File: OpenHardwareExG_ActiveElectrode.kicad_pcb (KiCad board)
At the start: 2 copper layers, 19.1 x 19.1 mm, 13 parts, among them K1 CONN_3, P1 CONN_1, U1 LMP7715, U2 LMP7721

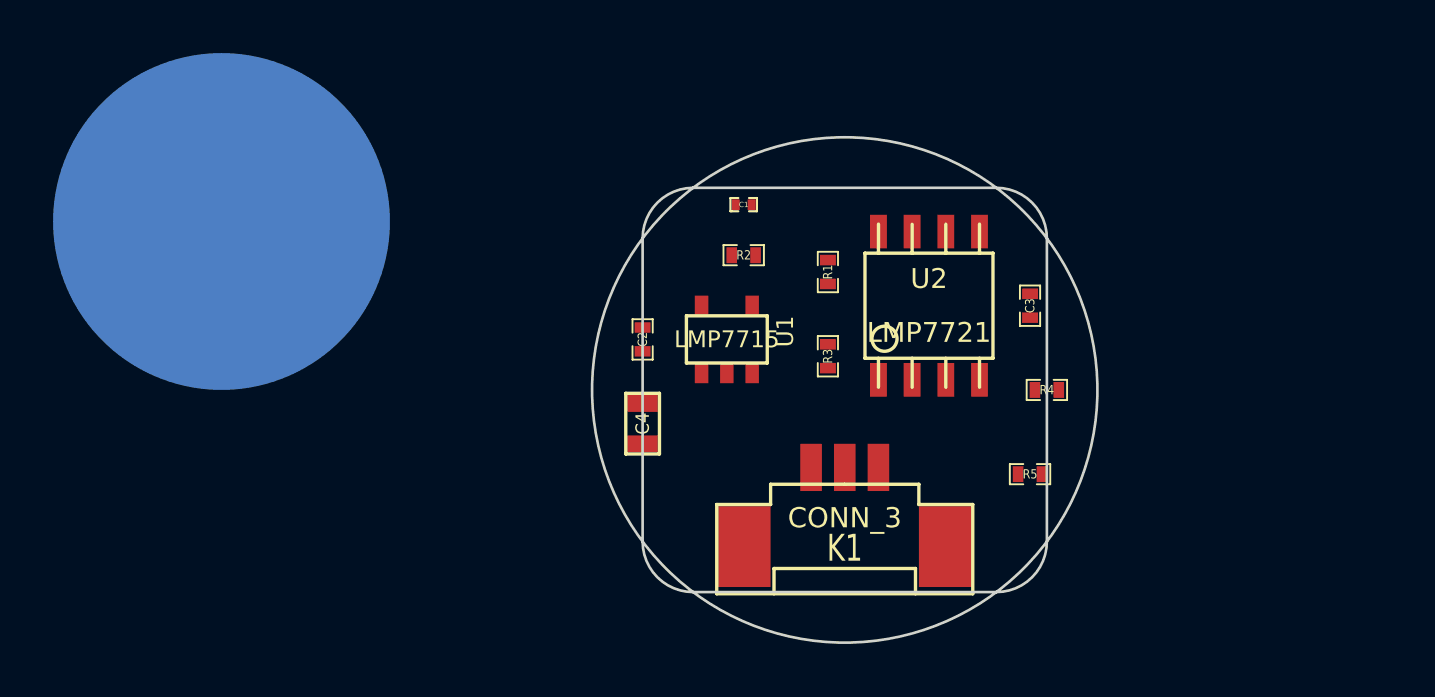
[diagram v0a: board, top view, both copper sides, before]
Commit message: improved draft of component positions
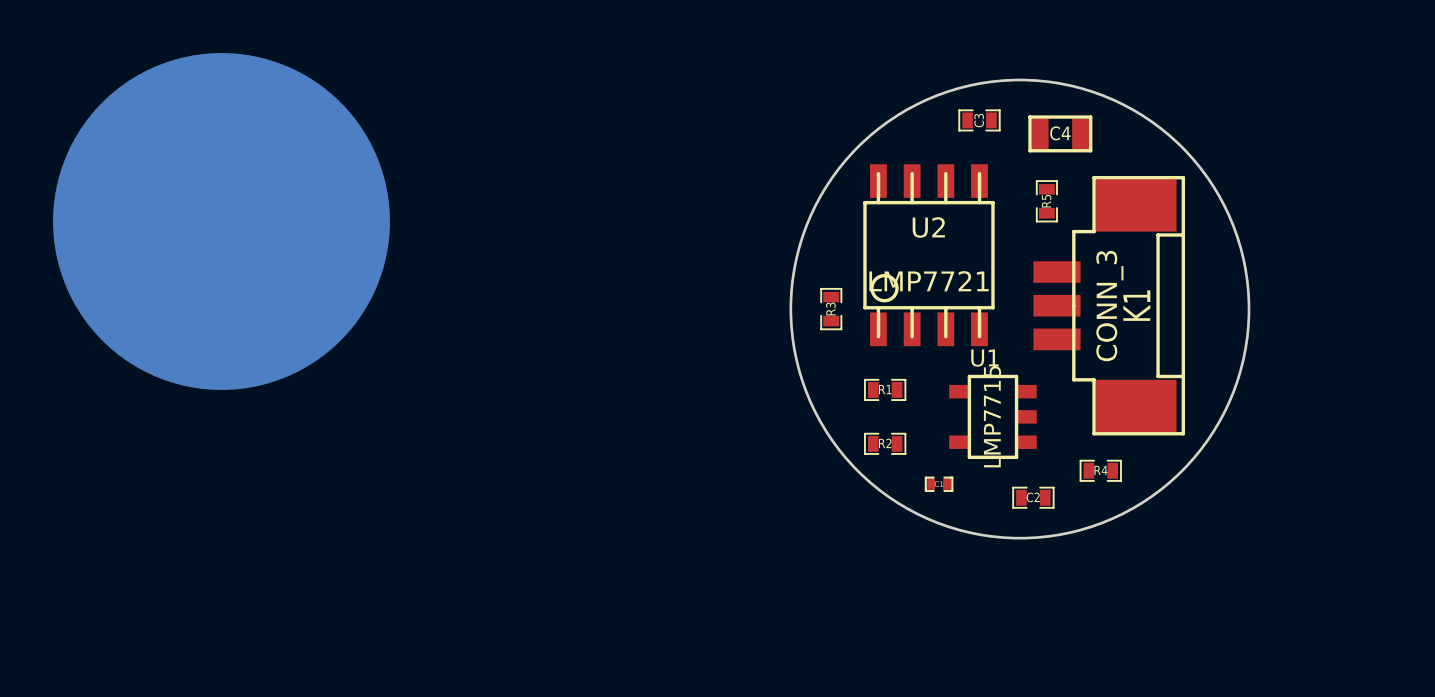
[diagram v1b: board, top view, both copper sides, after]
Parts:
- moved C4 19.2 mm to (109.7, 43.7), turned to 0 degrees
- moved C2 15.9 mm to (108.7, 57.4), turned to 0 degrees
- moved K1 14.9 mm to (113.0, 50.2), turned to 90 degrees
- moved C1 12.9 mm to (105.2, 56.9), turned to 0 degrees
- moved U1 10.4 mm to (107.2, 54.4), turned to 90 degrees
- moved R5 10.3 mm to (109.2, 46.2), turned to 270 degrees
- moved R2 8.89 mm to (103.1, 55.4), turned to 0 degrees
- moved C3 7.24 mm to (106.7, 43.2), turned to 0 degrees
- moved R1 4.94 mm to (103.1, 53.3), turned to 180 degrees
- moved R4 3.66 mm to (111.3, 56.4)
- moved U2 1.91 mm to (104.8, 48.3)
- moved R3 1.78 mm to (101.1, 50.3), turned to 270 degrees
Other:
- board size 19.1 x 19.1 mm -> 17.3 x 17.3 mm

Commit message: experiment with 0.1" connector (too large)
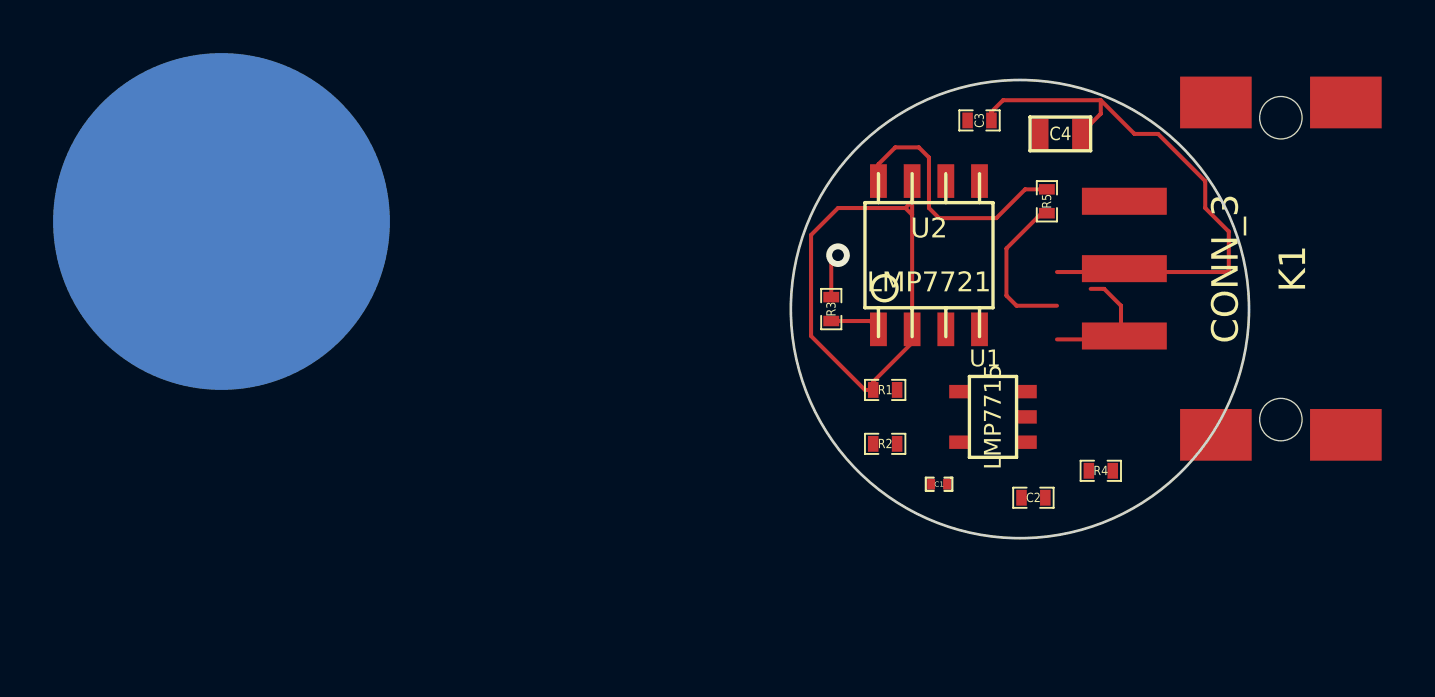
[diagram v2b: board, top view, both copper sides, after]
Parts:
- K1: footprint CONN3_SMD -> 3PIN_SMD_ERNI
- moved K1 1.66 mm to (112.1, 48.8), turned to 270 degrees
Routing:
- net GND: track 0.00 -> 26.6 mm
- net /GUARD_RING: track 0.00 -> 20.9 mm
- net /BUFFERED_INPUT: track 0.00 -> 9.92 mm
- net /LINE_OUT: track 0.00 -> 5.92 mm
- net /PROTECTED_ELECTRODE: track 0.00 -> 1.91 mm
- net /ELECTRODE: track 0.00 -> 1.69 mm, vias 0 -> 1
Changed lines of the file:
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@@
   (general
     (links 24)
-    (no_connects 24)
+    (no_connects 19)
     (area 0 0 0 0)
     (thickness 1.6)
     (drawings 1)
-    (tracks 0)
+    (tracks 49)
     (zones 0)
     (modules 13)
@@
     (mod_text_size 1 1)
     (mod_text_width 0.15)
-    (pad_size 12.7 12.7)
-    (pad_drill 0)
+    (pad_size 1.6 1.6)
+    (pad_drill 1.6)
     (pad_to_mask_clearance 0)
     (aux_axis_origin 0 0)
@@
     )
   )
-  (module CONN3_SMD (layer F.Cu)
-    (at 113.03 50.165 90)
-    (attr smd)
-    (fp_text reference K1 (at 0 -0.381 90) (layer F.SilkS)
-      (effects (font (size 1.016 0.762) (thickness 0.1524)))
-    )
-    (fp_text value CONN_3 (at 0 -1.524 90) (layer F.SilkS)
-      (effects (font (size 0.762 0.762) (thickness 0.1524)))
-    )
-    (fp_line (start 2.667 1.3335) (end 2.667 0.381) (layer F.SilkS) (width 0.127))
-    (fp_line (start 2.667 0.381) (end -2.667 0.381) (layer F.SilkS) (width 0.127))
-    (fp_line (start -2.667 0.381) (end -2.667 1.3335) (layer F.SilkS) (width 0.127))
-    (fp_line (start 0 -2.794) (end 2.794 -2.794) (layer F.SilkS) (width 0.127))
-    (fp_line (start 2.794 -2.794) (end 2.794 -2.032) (layer F.SilkS) (width 0.127))
-    (fp_line (start 2.794 -2.032) (end 4.826 -2.032) (layer F.SilkS) (width 0.127))
-    (fp_line (start 4.826 -2.032) (end 4.826 1.3335) (layer F.SilkS) (width 0.127))
-    (fp_line (start 4.826 1.3335) (end -4.826 1.3335) (layer F.SilkS) (width 0.127))
-    (fp_line (start -4.826 1.3335) (end -4.826 -2.032) (layer F.SilkS) (width 0.127))
-    (fp_line (start -4.826 -2.032) (end -2.794 -2.032) (layer F.SilkS) (width 0.127))
-    (fp_line (start -2.794 -2.032) (end -2.794 -2.794) (layer F.SilkS) (width 0.127))
-    (fp_line (start -2.794 -2.794) (end 0 -2.794) (layer F.SilkS) (width 0.127))
-    (pad 3 smd rect (at 1.27 -3.429 90) (size 0.8128 1.778)
-      (layers F.Cu F.Paste F.Mask)
-      (net 10 GND)
-    )
-    (pad 2 smd rect (at 0 -3.429 90) (size 0.8128 1.778)
-      (layers F.Cu F.Paste F.Mask)
-      (net 8 /LINE_OUT)
-    )
-    (pad 1 smd rect (at -1.27 -3.429 90) (size 0.8128 1.778)
-      (layers F.Cu F.Paste F.Mask)
-      (net 1 +5V)
-    )
-    (pad "" smd rect (at 3.81 -0.4445 90) (size 2.032 3.048)
-      (layers F.Cu F.Paste F.Mask)
-    )
-    (pad "" smd rect (at -3.81 -0.4445 90) (size 2.032 3.048)
-      (layers F.Cu F.Paste F.Mask)
-    )
-    (model smd/conn3_smd.wrl
-      (at (xyz 0 0 0))
-      (scale (xyz 0.4 0.4 0.4))
-      (rotate (xyz 0 0 0))
-    )
-  )
   (module electrode_pad (layer B.Cu)
     (at 78.105 46.99)
@@
     )
   )
+  (module 3PIN_SMD_ERNI (layer F.Cu)
+    (at 112.141 48.768 270)
+    (fp_text reference K1 (at 0 -6.35 270) (layer F.SilkS)
+      (effects (font (size 1 1) (thickness 0.15)))
+    )
+    (fp_text value CONN_3 (at 0 -3.81 270) (layer F.SilkS)
+      (effects (font (size 1 1) (thickness 0.15)))
+    )
+    (pad 2 smd rect (at 0 0 270) (size 1.02 3.2)
+      (layers F.Cu F.Paste F.Mask)
+      (net 8 /LINE_OUT)
+    )
+    (pad 3 smd rect (at 2.54 0 270) (size 1.02 3.2)
+      (layers F.Cu F.Paste F.Mask)
+      (net 10 GND)
+    )
+    (pad 1 smd rect (at -2.54 0 270) (size 1.02 3.2)
+      (layers F.Cu F.Paste F.Mask)
+      (net 1 +5V)
+    )
+    (pad "" smd rect (at -6.265 -3.45 270) (size 1.95 2.7)
+      (layers F.Cu F.Paste F.Mask)
+    )
+    (pad "" smd rect (at 6.265 -3.45 270) (size 1.95 2.7)
+      (layers F.Cu F.Paste F.Mask)
+    )
+    (pad "" smd rect (at -6.265 -8.35 270) (size 1.95 2.7)
+      (layers F.Cu F.Paste F.Mask)
+    )
+    (pad "" smd rect (at 6.265 -8.35 270) (size 1.95 2.7)
+      (layers F.Cu F.Paste F.Mask)
+    )
+    (pad "" np_thru_hole circle (at -5.69 -5.9 270) (size 1.6 1.6) (drill 1.6)
+      (layers *.Cu *.Mask F.SilkS)
+    )
+    (pad "" np_thru_hole circle (at 5.69 -5.9 270) (size 1.6 1.6) (drill 1.6)
+      (layers *.Cu *.Mask F.SilkS)
+    )
+  )
   (gr_circle (center 108.204 50.292) (end 108.204 58.928) (layer Edge.Cuts) (width 0.1))
+  (segment (start 102.87 45.466) (end 102.87 44.831) (width 0.1524) (layer F.Cu) (net 2))
+  (segment (start 108.39958 45.77842) (end 109.22 45.77842) (width 0.1524) (layer F.Cu) (net 2))
+  (segment (start 107.315 46.863) (end 108.39958 45.77842) (width 0.1524) (layer F.Cu) (net 2))
+  (segment (start 105.156 46.863) (end 107.315 46.863) (width 0.1524) (layer F.Cu) (net 2))
+  (segment (start 104.775 46.482) (end 105.156 46.863) (width 0.1524) (layer F.Cu) (net 2))
+  (segment (start 104.775 44.577) (end 104.775 46.482) (width 0.1524) (layer F.Cu) (net 2))
+  (segment (start 104.394 44.196) (end 104.775 44.577) (width 0.1524) (layer F.Cu) (net 2))
+  (segment (start 103.505 44.196) (end 104.394 44.196) (width 0.1524) (layer F.Cu) (net 2))
+  (segment (start 102.87 44.831) (end 103.505 44.196) (width 0.1524) (layer F.Cu) (net 2))
+  (segment (start 101.092 49.84242) (end 101.092 48.514) (width 0.1524) (layer F.Cu) (net 3))
+  (via (at 101.346 48.26) (size 0.889) (layers F.Cu B.Cu) (net 3))
+  (segment (start 101.092 48.514) (end 101.346 48.26) (width 0.1524) (layer F.Cu) (net 3))
+  (segment (start 103.886 46.482) (end 104.14 46.736) (width 0.1524) (layer F.Cu) (net 4))
+  (segment (start 104.14 51.054) (end 104.14 46.736) (width 0.1524) (layer F.Cu) (net 4))
+  (segment (start 104.14 46.736) (end 104.14 45.466) (width 0.1524) (layer F.Cu) (net 4))
+  (segment (start 102.67442 53.34) (end 102.362 53.34) (width 0.1524) (layer F.Cu) (net 4))
+  (segment (start 102.362 53.34) (end 100.33 51.308) (width 0.1524) (layer F.Cu) (net 4))
+  (segment (start 100.33 51.308) (end 100.33 47.498) (width 0.1524) (layer F.Cu) (net 4))
+  (segment (start 100.33 47.498) (end 101.346 46.482) (width 0.1524) (layer F.Cu) (net 4))
+  (segment (start 101.346 46.482) (end 103.886 46.482) (width 0.1524) (layer F.Cu) (net 4))
+  (segment (start 103.886 46.482) (end 104.14 46.228) (width 0.1524) (layer F.Cu) (net 4))
+  (segment (start 104.14 46.228) (end 104.14 45.466) (width 0.1524) (layer F.Cu) (net 4))
+  (segment (start 104.14 51.054) (end 104.14 51.562) (width 0.1524) (layer F.Cu) (net 4))
+  (segment (start 102.67442 53.02758) (end 102.67442 53.34) (width 0.1524) (layer F.Cu) (net 4))
+  (segment (start 104.14 51.562) (end 102.67442 53.02758) (width 0.1524) (layer F.Cu) (net 4))
+  (segment (start 109.22 46.67758) (end 109.02442 46.67758) (width 0.1524) (layer F.Cu) (net 8))
+  (segment (start 108.077 50.165) (end 109.601 50.165) (width 0.1524) (layer F.Cu) (net 8))
+  (segment (start 107.696 49.784) (end 108.077 50.165) (width 0.1524) (layer F.Cu) (net 8))
+  (segment (start 107.696 48.006) (end 107.696 49.784) (width 0.1524) (layer F.Cu) (net 8))
+  (segment (start 109.02442 46.67758) (end 107.696 48.006) (width 0.1524) (layer F.Cu) (net 8))
+  (segment (start 101.092 50.74158) (end 102.55758 50.74158) (width 0.1524) (layer F.Cu) (net 9))
+  (segment (start 102.55758 50.74158) (end 102.87 51.054) (width 0.1524) (layer F.Cu) (net 9))
+  (segment (start 109.601 51.435) (end 111.633 51.435) (width 0.1524) (layer F.Cu) (net 10))
+  (segment (start 111.379 49.53) (end 110.871 49.53) (width 0.1524) (layer F.Cu) (net 10))
+  (segment (start 112.014 50.165) (end 111.379 49.53) (width 0.1524) (layer F.Cu) (net 10))
+  (segment (start 112.014 51.054) (end 112.014 50.165) (width 0.1524) (layer F.Cu) (net 10))
+  (segment (start 111.633 51.435) (end 112.014 51.054) (width 0.1524) (layer F.Cu) (net 10))
+  (segment (start 107.12958 43.18) (end 107.12958 42.85742) (width 0.1524) (layer F.Cu) (net 10))
+  (segment (start 107.569 42.418) (end 111.252 42.418) (width 0.1524) (layer F.Cu) (net 10))
+  (segment (start 107.12958 42.85742) (end 107.569 42.418) (width 0.1524) (layer F.Cu) (net 10))
+  (segment (start 109.601 48.895) (end 116.078 48.895) (width 0.1524) (layer F.Cu) (net 10))
+  (segment (start 111.252 42.926) (end 110.49 43.688) (width 0.1524) (layer F.Cu) (net 10))
+  (segment (start 111.252 42.418) (end 111.252 42.926) (width 0.1524) (layer F.Cu) (net 10))
+  (segment (start 112.522 43.688) (end 111.252 42.418) (width 0.1524) (layer F.Cu) (net 10))
+  (segment (start 113.411 43.688) (end 112.522 43.688) (width 0.1524) (layer F.Cu) (net 10))
+  (segment (start 115.189 45.466) (end 113.411 43.688) (width 0.1524) (layer F.Cu) (net 10))
+  (segment (start 115.189 46.482) (end 115.189 45.466) (width 0.1524) (layer F.Cu) (net 10))
+  (segment (start 116.078 47.371) (end 115.189 46.482) (width 0.1524) (layer F.Cu) (net 10))
+  (segment (start 116.078 48.895) (end 116.078 47.371) (width 0.1524) (layer F.Cu) (net 10))
 )

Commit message: finish initial PCB layout
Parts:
- C1: footprint SM0201_r -> Capacitors_SMD:C_0201
- C2, C3: footprint SM0402 -> Capacitors_SMD:C_0402
- C4: footprint SM0603 -> Capacitors_SMD:C_0603
- K1: footprint 3PIN_SMD_ERNI -> active_electrode_connectors:DF50A-3P-1H
- P1: footprint electrode_pad -> electrode_pad:electrode_pad
- R1, R2, R3, R4, R5: footprint SM0402 -> Resistors_SMD:R_0402
- U1: footprint SOT23-5 -> TO_SOT_Packages_SMD:SOT-23-5
- U2: footprint so-8 -> Housings_SOIC:SOIC-8_3.9x4.9mm_Pitch1.27mm
- moved P1 23.8 mm to (101.6, 50.8)
- moved R5 12.2 mm to (97.2, 44.5), turned to 0 degrees
- moved K1 10.0 mm to (102.2, 50.2), turned to 90 degrees
- moved C4 9.77 mm to (100.3, 46.4)
- moved U2 9.25 mm to (95.9, 50.8), turned to 90 degrees
- moved R4 9.19 mm to (102.2, 54.6), turned to 180 degrees
- moved C2 8.43 mm to (100.3, 56.5), turned to 270 degrees
- moved R3 8.11 mm to (95.9, 56.5)
- moved C1 7.42 mm to (97.8, 57.8)
- moved R1 6.66 mm to (99.7, 59.1), turned to 270 degrees
- moved C3 6.48 mm to (100.3, 44.5)
- moved U1 5.51 mm to (102.9, 57.8)
- moved R2 4.73 mm to (98.4, 55.9)
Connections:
- K1 pad : (no net) -> /GUARD_RING
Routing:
- net /GUARD_RING: track 20.9 -> 50.5 mm, vias 0 -> 4
- net +5V: track 0.00 -> 21.1 mm
- net GND: track 26.6 -> 35.8 mm
- net /GUARD_RING_FILTERED_FEEDBACK: track 0.00 -> 8.76 mm
- net /BUFFERED_INPUT: track 9.92 -> 18.1 mm
- net /GUARD_RING_DRIVER: track 0.00 -> 7.20 mm
- net /LINE_OUT: track 5.92 -> 11.6 mm
- net /GUARD_RING_INPUT: track 0.00 -> 5.63 mm
- net /PROTECTED_ELECTRODE: track 1.91 -> 4.25 mm
- net /ELECTRODE: track 1.69 -> 0.98 mm
- added copper zone on B.Cu, net /GUARD_RING
- added copper zone on F.Cu, net /GUARD_RING
- added copper zone on In1.Cu, net /GUARD_RING
- added copper zone on In2.Cu, net /GUARD_RING
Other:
- board size 17.3 x 17.3 mm -> 19.3 x 19.3 mm
- copper layers 2 -> 4
